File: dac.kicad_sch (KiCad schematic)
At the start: 23 parts, among them U10 L78L05_SOT89, U9 AK4454

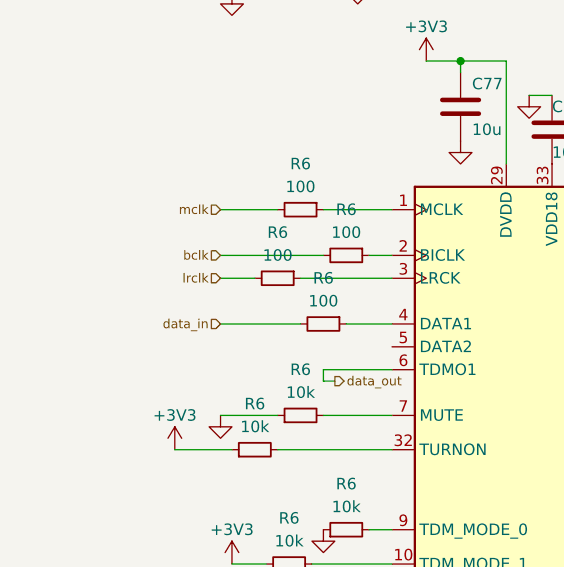
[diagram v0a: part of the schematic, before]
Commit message: add dsp and esp32... schematic mostly done
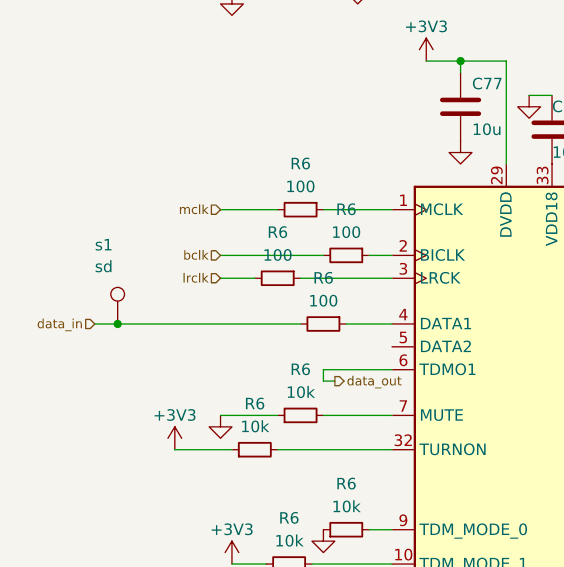
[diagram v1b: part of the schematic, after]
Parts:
- added s1: sd, invendelirium_general:pad_1.2x1.5, symbol Connector:TestPoint
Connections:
- net data_in: now also s1.1
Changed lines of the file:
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@@
   (junction (at 99.06 119.38) (diameter 0) (color 0 0 0 0)
   )
+  (junction (at 90.17 73.66) (diameter 0) (color 0 0 0 0)
+  )
   (junction (at 99.06 115.57) (diameter 0) (color 0 0 0 0)
   )
@@
     (stroke (width 0) (type default))
   )
+  (wire (pts (xy 90.17 73.66) (xy 110.49 73.66))
+    (stroke (width 0) (type default))
+  )
   (wire (pts (xy 199.39 80.01) (xy 201.93 80.01))
     (stroke (width 0) (type default))
@@
     (stroke (width 0) (type default))
   )
-  (wire (pts (xy 101.6 73.66) (xy 110.49 73.66))
+  (wire (pts (xy 87.63 73.66) (xy 90.17 73.66))
     (stroke (width 0) (type default))
   )
@@
     (effects (font (size 1.016 1.016)) (justify left))
   )
-  (hierarchical_label "data_in" (shape input) (at 101.6 73.66 180) (fields_autoplaced)
+  (hierarchical_label "data_in" (shape input) (at 87.63 73.66 180) (fields_autoplaced)
     (effects (font (size 1.016 1.016)) (justify right))
   )
@@
         )
       )
+    )
+  )
+  (symbol (lib_id "Connector:TestPoint") (at 90.17 73.66 0) (unit 1)
+    (in_bom yes) (on_board yes) (dnp no)
+    (property "Reference" "s1" (at 87.63 64.897 0)
+      (effects (font (size 1.27 1.27)) (justify left))
+    )
+    (property "Value" "sd" (at 87.63 67.31 0)
+      (effects (font (size 1.27 1.27)) (justify left))
+    )
+    (property "Footprint" "invendelirium_general:pad_1.2x1.5" (at 95.25 73.66 0)
+      (effects (font (size 1.27 1.27)) hide)
+    )
+    (property "Datasheet" "~" (at 95.25 73.66 0)
+      (effects (font (size 1.27 1.27)) hide)
+    )
+    (pin "1")
+    (instances
+      (project "uberamp1"
+        (path "/310059c1-d84b-43e2-9c9a-0e426c534a12/c6ef957f-dbb4-496d-aec2-44492c2243c4"
+          (reference "s1") (unit 1)
+        )
+        (path "/310059c1-d84b-43e2-9c9a-0e426c534a12/1727f815-1282-4ad8-874c-d1f66f4d7fbe"
+          (reference "s3") (unit 1)
+        )
+        (path "/310059c1-d84b-43e2-9c9a-0e426c534a12/e09aca01-5377-42b6-85e8-8afbf1155690"
+          (reference "s5") (unit 1)
+        )
+        (path "/310059c1-d84b-43e2-9c9a-0e426c534a12/b23c2595-3b45-43cf-b3fd-b0c94e6d7f84"
+          (reference "s7") (unit 1)
+        )
+        (path "/310059c1-d84b-43e2-9c9a-0e426c534a12/9f0654db-0c52-4f70-8768-bb44a6ed6168"
+          (reference "s10") (unit 1)
+        )
+        (path "/310059c1-d84b-43e2-9c9a-0e426c534a12/9338c448-a5fc-4246-a946-e7fc08f9b36f"
+          (reference "s23") (unit 1)
+        )
+        (path "/310059c1-d84b-43e2-9c9a-0e426c534a12/7069641c-0ed4-4995-a63e-1f44999c4edd"
+          (reference "s24") (unit 1)
+        )
+      )

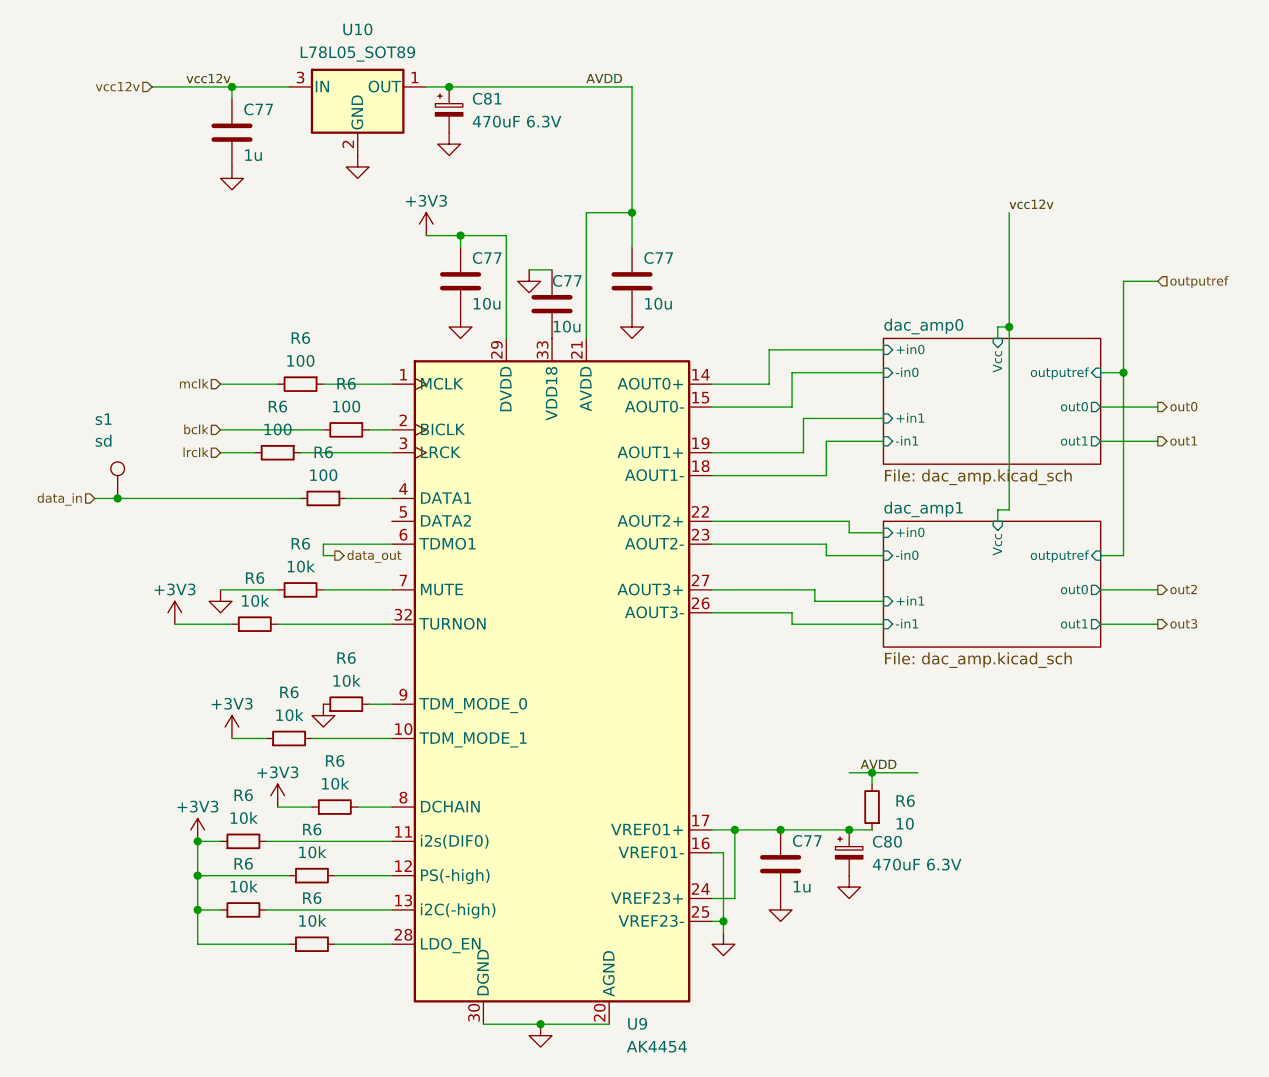
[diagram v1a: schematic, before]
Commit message: update to kicad 8
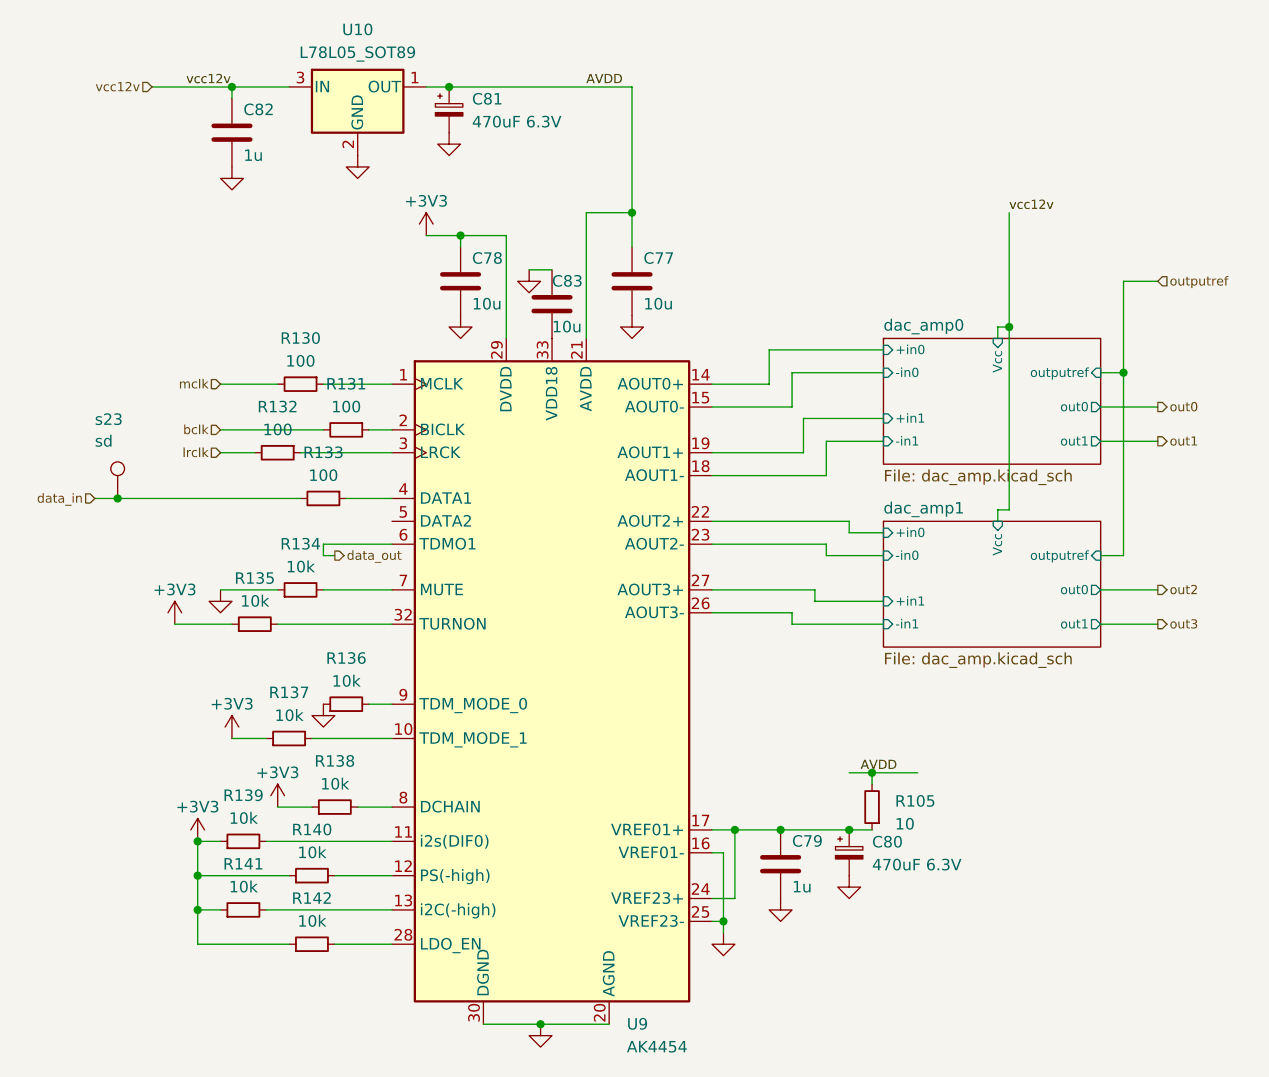
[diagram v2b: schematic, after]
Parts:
- renumbered C77 to C78, C77 to C79, C77 to C82, C77 to C83, R6 to R105, R6 to R130, R6 to R131, R6 to R132, R6 to R133, R6 to R134, R6 to R135, R6 to R136, R6 to R137, R6 to R138, R6 to R139, R6 to R140, R6 to R141, R6 to R142, s1 to s23

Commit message: schematic: some fixes
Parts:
- added R220: 10k, invendelirium_audio:R_0603, symbol Device:R_Small
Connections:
- net GND: now also R220.1
- net at U9.5 (DATA2): now also R220.2
- net +3V3 renamed 3V3
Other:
- moved on the sheet: C83

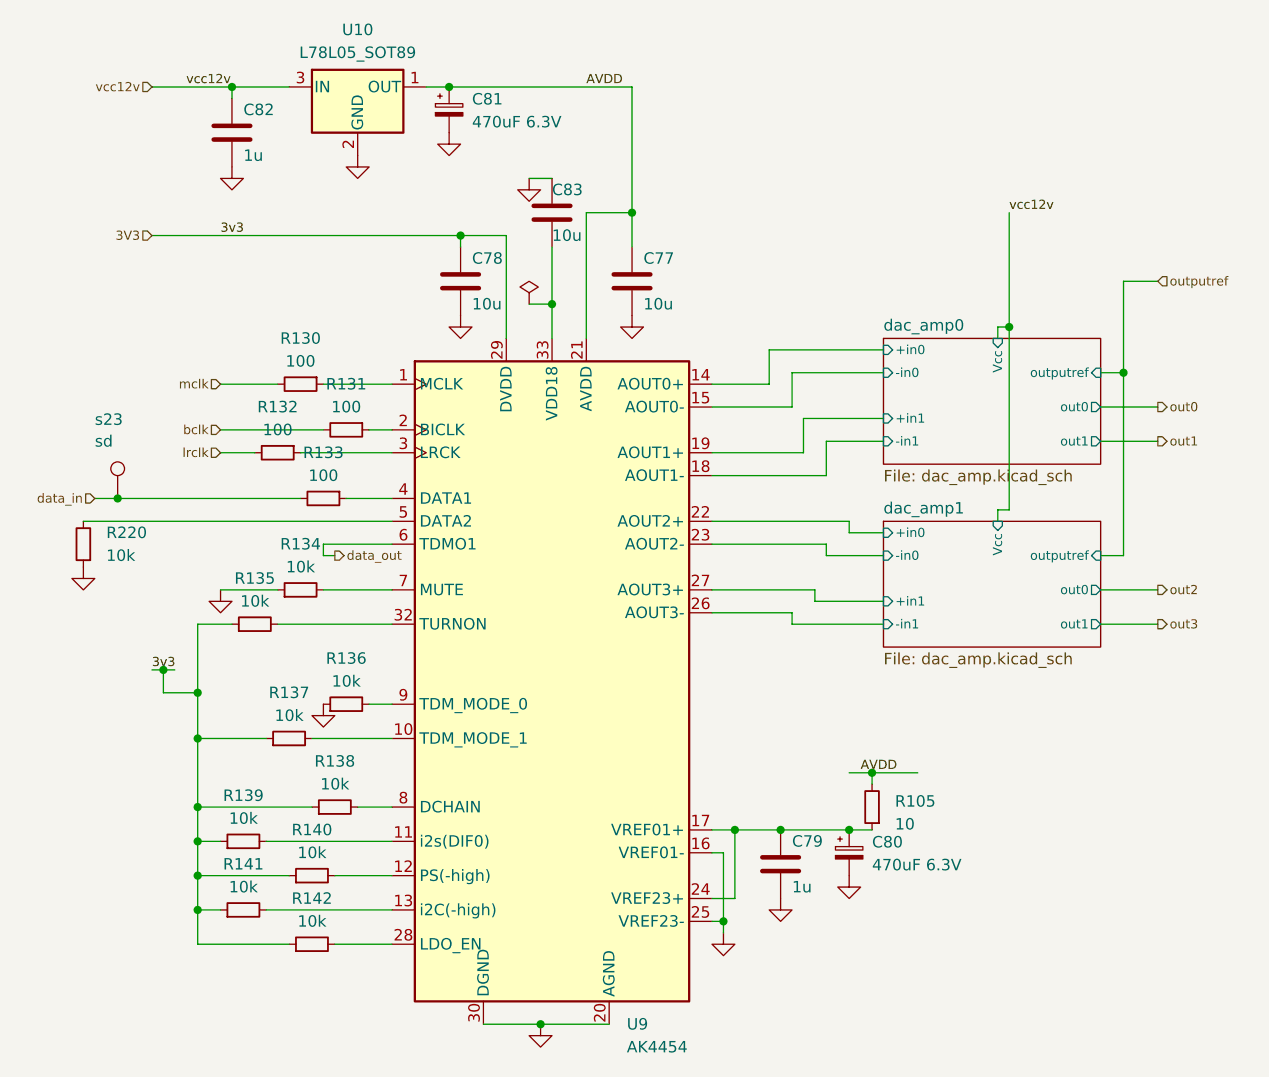
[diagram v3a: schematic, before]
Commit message: add power input +...
+ tons of fixes, footprint assignments, etc
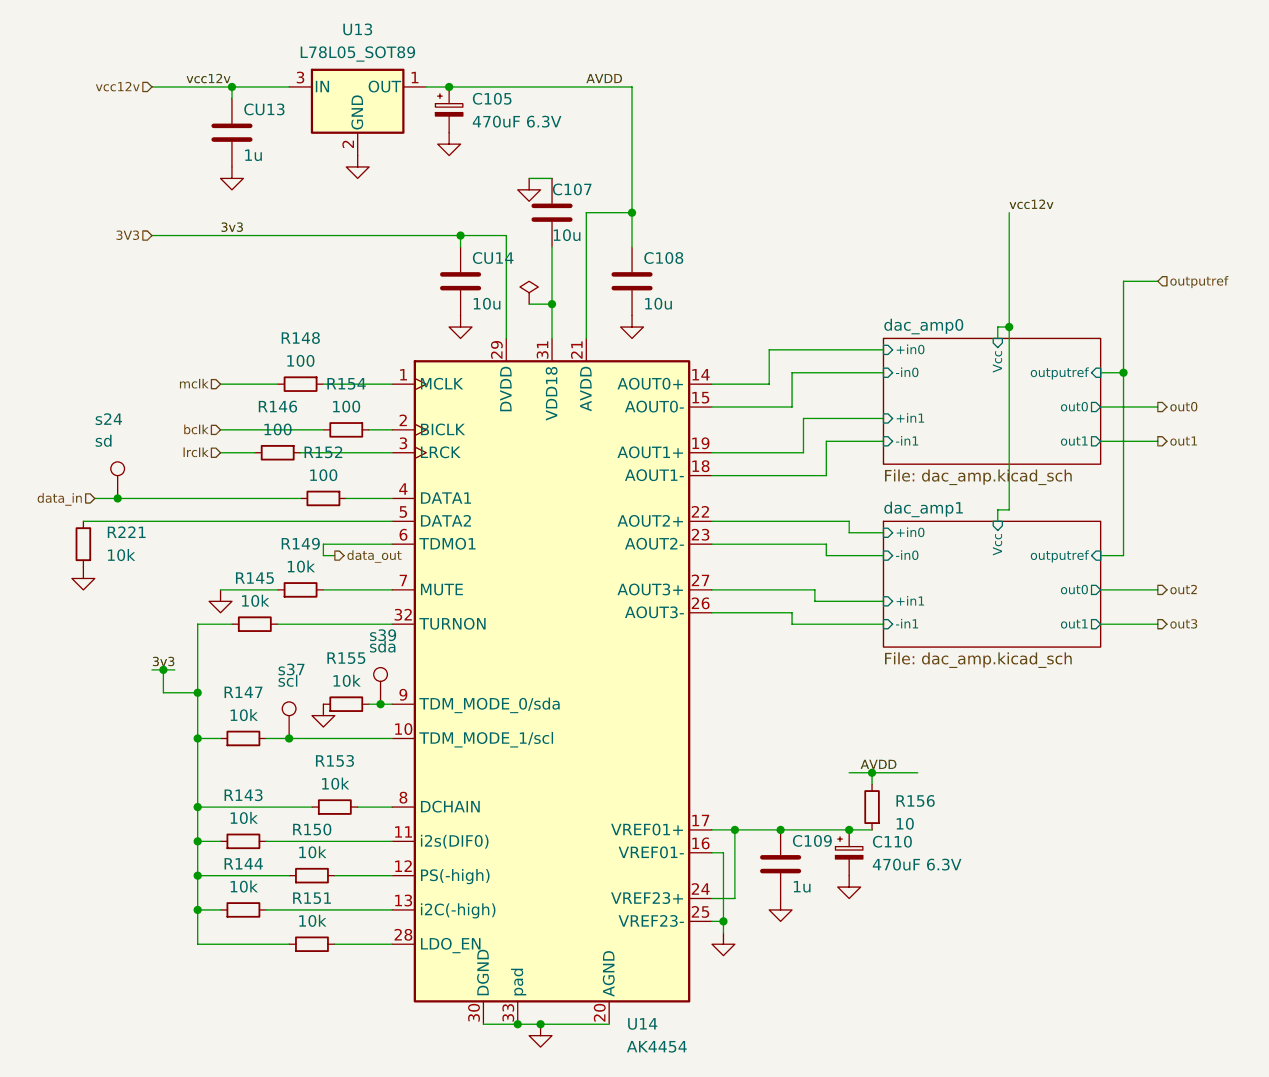
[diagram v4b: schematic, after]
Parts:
- added s37: scl, invendelirium_general:pad_1.2x1.5, symbol Connector:TestPoint
- added s39: sda, invendelirium_general:pad_1.2x1.5, symbol Connector:TestPoint
- C105: renamed from C81; footprint (none) -> invendelirium_general:CP_Radial_D8.0mm_P3.50mm; PN (none) -> A759EK477M0JAAE016
- C110: renamed from C80; footprint (none) -> invendelirium_general:CP_Radial_D8.0mm_P3.50mm; PN (none) -> A759EK477M0JAAE016
- U14: renamed from U9; footprint (none) -> invendelirium_audio:QFN-8p8p-5x5mm
- renumbered C83 to C107, C77 to C108, C79 to C109, C82 to CU13, C78 to CU14, R139 to R143, R141 to R144, R135 to R145, R132 to R146, R137 to R147, R130 to R148, R134 to R149, R140 to R150, R142 to R151, R133 to R152, R138 to R153, R131 to R154, R136 to R155, R105 to R156, R220 to R221, U10 to U13, s23 to s24
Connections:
- net GND: now also U14.33 (pad)
- net at C107.2: now also U14.31 (VDD18); no longer U14.33 (VDD18)
- net at R155.2, U14.9 (TDM_MODE_0/sda): now also s39.1
- net at R147.2, U14.10 (TDM_MODE_1/scl): now also s37.1
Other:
- moved on the sheet: R147

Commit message: some routing till got stuck
got stuck on U16's power part somehow being on a different sheet
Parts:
- renumbered s37 to s38, s39 to s40
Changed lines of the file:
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@@
 		(on_board yes)
 		(dnp no)
-		(property "Reference" "s39"
+		(property "Reference" "s40"
 			(at 118.11 88.9 0)
 			(effects
@@
 		(on_board yes)
 		(dnp no)
-		(property "Reference" "s37"
+		(property "Reference" "s38"
 			(at 107.95 92.71 0)
 			(effects
